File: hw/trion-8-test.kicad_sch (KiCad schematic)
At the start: 4 parts

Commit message: cleanup of trion project
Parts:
- removed H1, H2, H3, H4: Foot FF-13-P3.5X5.5B, proj_footprints:foot_ff-13, symbol Mechanical:MountingHole
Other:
- removed sheet Ethernet
- removed sheet GPS
- removed sheet LED
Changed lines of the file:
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@@
 (kicad_sch (version 20230121) (generator eeschema)
   (paper "A4")
-  (symbol (lib_id "Mechanical:MountingHole") (at 191.77 132.08 0) (unit 1)
-    (in_bom yes) (on_board yes) (dnp no)
-    (property "Reference" "H3" (at 194.31 130.8679 0)
-      (effects (font (size 1.27 1.27)) (justify left))
-    )
-    (property "Value" "Foot FF-13-P3.5X5.5B" (at 180.34 142.24 0)
-      (effects (font (size 1.27 1.27)) (justify left))
-    )
-    (property "Footprint" "proj_footprints:foot_ff-13" (at 191.77 132.08 0)
-      (effects (font (size 1.27 1.27)) hide)
-    )
-    (property "Datasheet" "~" (at 191.77 132.08 0)
-      (effects (font (size 1.27 1.27)) hide)
-    )
-    (property "Part" "FF-13-P3.5X5.5B" (at 191.77 132.08 0)
-      (effects (font (size 1.27 1.27)) hide)
-    )
-    (property "Manufacturer" "Essentra" (at 191.77 132.08 0)
-      (effects (font (size 1.27 1.27)) hide)
-    )
-    (instances
-      (project "trion-8-test"
-        (path "/8c6e15e3-1804-4f03-8a4f-3cb8420d9169"
-          (reference "H3") (unit 1)
-        )
-      )
-    )
-  )
-  (symbol (lib_id "Mechanical:MountingHole") (at 171.45 132.08 0) (unit 1)
-    (in_bom yes) (on_board yes) (dnp no)
-    (property "Reference" "H1" (at 173.99 130.8679 0)
-      (effects (font (size 1.27 1.27)) (justify left))
-    )
-    (property "Value" "Foot FF-13-P3.5X5.5B" (at 160.02 136.525 0)
-      (effects (font (size 1.27 1.27)) (justify left))
-    )
-    (property "Footprint" "proj_footprints:foot_ff-13" (at 171.45 132.08 0)
-      (effects (font (size 1.27 1.27)) hide)
-    )
-    (property "Datasheet" "~" (at 171.45 132.08 0)
-      (effects (font (size 1.27 1.27)) hide)
-    )
-    (property "Part" "FF-13-P3.5X5.5B" (at 171.45 132.08 0)
-      (effects (font (size 1.27 1.27)) hide)
-    )
-    (property "Manufacturer" "Essentra" (at 171.45 132.08 0)
-      (effects (font (size 1.27 1.27)) hide)
-    )
-    (instances
-      (project "trion-8-test"
-        (path "/8c6e15e3-1804-4f03-8a4f-3cb8420d9169"
-          (reference "H1") (unit 1)
-        )
-      )
-    )
-  )
-  (symbol (lib_id "Mechanical:MountingHole") (at 201.295 132.08 0) (unit 1)
-    (in_bom yes) (on_board yes) (dnp no)
-    (property "Reference" "H4" (at 203.835 130.8679 0)
-      (effects (font (size 1.27 1.27)) (justify left))
-    )
-    (property "Value" "Foot FF-13-P3.5X5.5B" (at 189.865 144.78 0)
-      (effects (font (size 1.27 1.27)) (justify left))
-    )
-    (property "Footprint" "proj_footprints:foot_ff-13" (at 201.295 132.08 0)
-      (effects (font (size 1.27 1.27)) hide)
-    )
-    (property "Datasheet" "~" (at 201.295 132.08 0)
-      (effects (font (size 1.27 1.27)) hide)
-    )
-    (property "Part" "FF-13-P3.5X5.5B" (at 201.295 132.08 0)
-      (effects (font (size 1.27 1.27)) hide)
-    )
-    (property "Manufacturer" "Essentra" (at 201.295 132.08 0)
-      (effects (font (size 1.27 1.27)) hide)
-    )
-    (instances
-      (project "trion-8-test"
-        (path "/8c6e15e3-1804-4f03-8a4f-3cb8420d9169"
-          (reference "H4") (unit 1)
-        )
-      )
-    )
-  )
-  (symbol (lib_id "Mechanical:MountingHole") (at 182.245 132.08 0) (unit 1)
-    (in_bom yes) (on_board yes) (dnp no)
-    (property "Reference" "H2" (at 184.785 130.8679 0)
-      (effects (font (size 1.27 1.27)) (justify left))
-    )
-    (property "Value" "Foot FF-13-P3.5X5.5B" (at 170.815 139.7 0)
-      (effects (font (size 1.27 1.27)) (justify left))
-    )
-    (property "Footprint" "proj_footprints:foot_ff-13" (at 182.245 132.08 0)
-      (effects (font (size 1.27 1.27)) hide)
-    )
-    (property "Datasheet" "~" (at 182.245 132.08 0)
-      (effects (font (size 1.27 1.27)) hide)
-    )
-    (property "Part" "FF-13-P3.5X5.5B" (at 182.245 132.08 0)
-      (effects (font (size 1.27 1.27)) hide)
-    )
-    (property "Manufacturer" "Essentra" (at 182.245 132.08 0)
-      (effects (font (size 1.27 1.27)) hide)
-    )
-    (instances
-      (project "trion-8-test"
-        (path "/8c6e15e3-1804-4f03-8a4f-3cb8420d9169"
-          (reference "H2") (unit 1)
-        )
-      )
-    )
-  )
   (sheet (at 96.52 108.585) (size 31.75 34.925) (fields_autoplaced)
     (stroke (width 0.1524) (type solid))
@@
       (project "trion-8-test"
         (path "/8c6e15e3-1804-4f03-8a4f-3cb8420d9169" (page "7"))
-      )
-    )
-  )
-  (sheet (at 162.56 44.45) (size 50.8 30.48) (fields_autoplaced)
-    (stroke (width 0.1524) (type solid))
-    (fill (color 0 0 0 0.0000))
-    (property "Sheetname" "Ethernet" (at 162.56 43.7384 0)
-      (effects (font (size 1.27 1.27)) (justify left bottom))
-    )
-    (property "Sheetfile" "ethernet.kicad_sch" (at 162.56 75.5146 0)
-      (effects (font (size 1.27 1.27)) (justify left top))
-    )
-    (instances
-      (project "trion-8-test"
-        (path "/8c6e15e3-1804-4f03-8a4f-3cb8420d9169" (page "8"))
-      )
-    )
-  )
-  (sheet (at 163.195 85.725) (size 49.53 32.385) (fields_autoplaced)
-    (stroke (width 0.1524) (type solid))
-    (fill (color 0 0 0 0.0000))
-    (property "Sheetname" "GPS" (at 163.195 85.0134 0)
-      (effects (font (size 1.27 1.27)) (justify left bottom))
-    )
-    (property "Sheetfile" "gps.kicad_sch" (at 163.195 118.6946 0)
-      (effects (font (size 1.27 1.27)) (justify left top))
-    )
-    (instances
-      (project "trion-8-test"
-        (path "/8c6e15e3-1804-4f03-8a4f-3cb8420d9169" (page "9"))
       )
     )
@@
       )
     )
-  )
-  (sheet (at 97.79 76.2) (size 33.655 19.685) (fields_autoplaced)
-    (stroke (width 0.1524) (type solid))
-    (fill (color 0 0 0 0.0000))
-    (property "Sheetname" "LED" (at 97.79 75.4884 0)
-      (effects (font (size 1.27 1.27)) (justify left bottom))
-    )
-    (property "Sheetfile" "led.kicad_sch" (at 97.79 96.4696 0)
-      (effects (font (size 1.27 1.27)) (justify left top))
-    )
-    (instances
-      (project "trion-8-test"
-        (path "/8c6e15e3-1804-4f03-8a4f-3cb8420d9169" (page "8"))
-      )
-    )

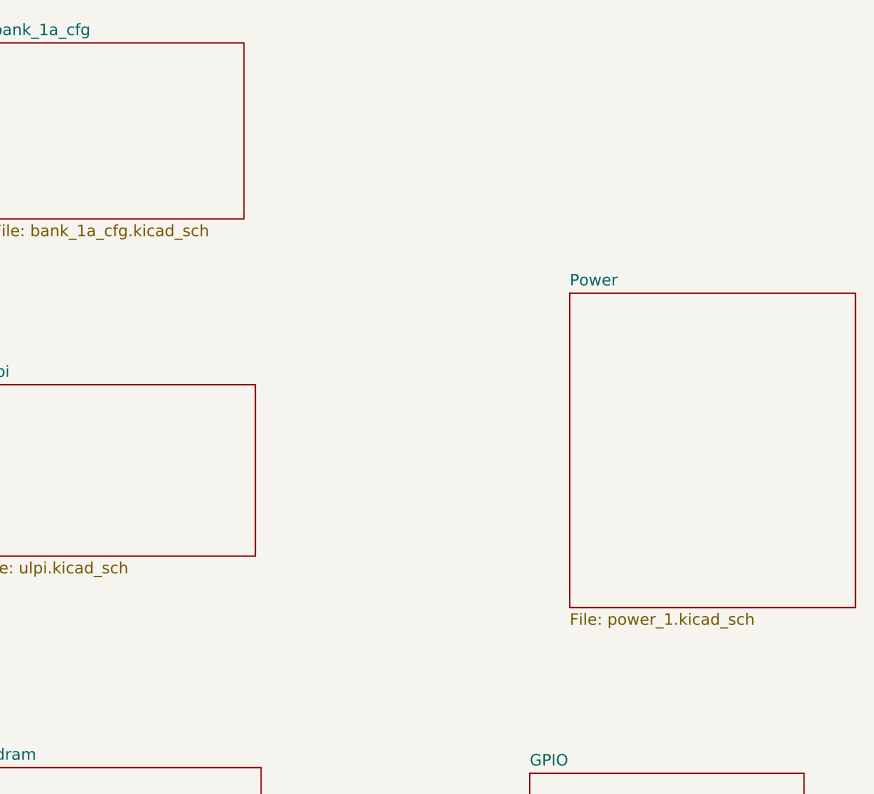
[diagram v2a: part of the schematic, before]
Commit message: layout almost complete with UPLI on the RHS => NO CLOCK INPUT
Have to rework and move the usb transceiver to the left...
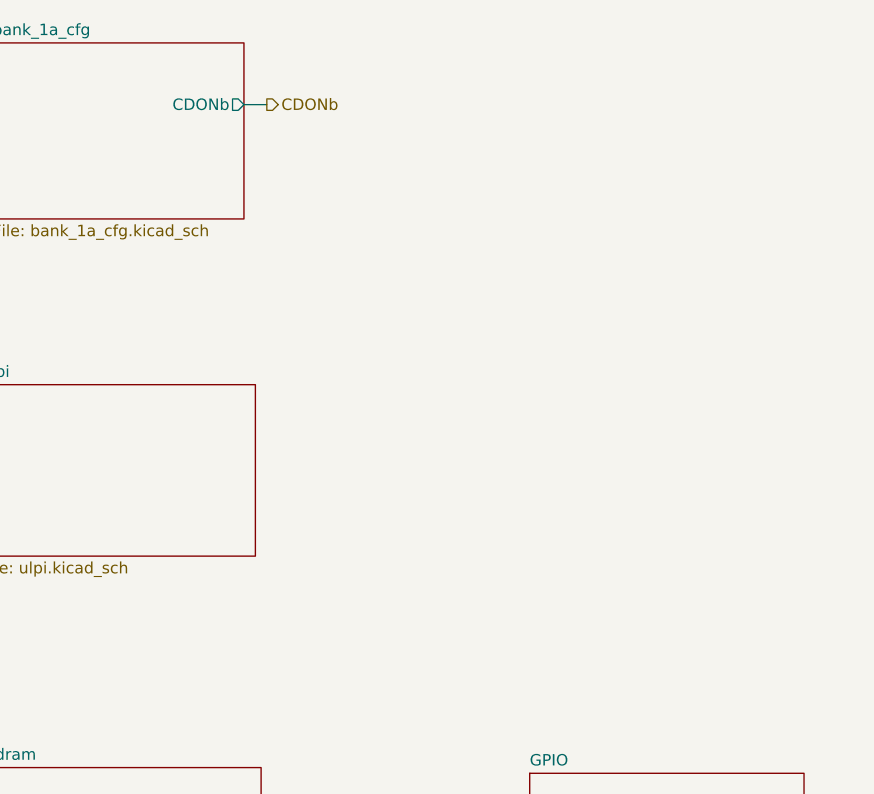
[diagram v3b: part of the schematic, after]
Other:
- removed sheet Power
- sheet bank_1a_cfg ports: added CDONb; removed none
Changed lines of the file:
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@@
 (kicad_sch (version 20230121) (generator eeschema)
   (paper "A4")
-  (sheet (at 96.52 108.585) (size 31.75 34.925) (fields_autoplaced)
-    (stroke (width 0.1524) (type solid))
-    (fill (color 0 0 0 0.0000))
-    (property "Sheetname" "Power" (at 96.52 107.8734 0)
-      (effects (font (size 1.27 1.27)) (justify left bottom))
-    )
-    (property "Sheetfile" "power_1.kicad_sch" (at 96.52 144.0946 0)
-      (effects (font (size 1.27 1.27)) (justify left top))
-    )
-    (instances
-      (project "trion-8-test"
-        (path "/8c6e15e3-1804-4f03-8a4f-3cb8420d9169" (page "7"))
-      )
-      (project "usbadc"
-        (path "/7c8a1f8d-8834-4c9b-aaae-1f231e9b09a1/d9cd2a48-41b0-4b01-a978-0843576735ad" (page "21"))
-      )
-    )
+  (wire (pts (xy 60.325 87.63) (xy 62.865 87.63))
+    (stroke (width 0) (type default))
+  )
+  (hierarchical_label "CDONb" (shape output) (at 62.865 87.63 0) (fields_autoplaced)
+    (effects (font (size 1.27 1.27)) (justify left))
   )
   (sheet (at 31.75 161.29) (size 30.48 24.13) (fields_autoplaced)
@@
       (effects (font (size 1.27 1.27)) (justify left top))
     )
+    (pin "CDONb" output (at 60.325 87.63 0)
+      (effects (font (size 1.27 1.27)) (justify right))
+    )
     (instances

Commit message: finalizing...
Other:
- sheet GPIO renamed bank_4a_4b
- sheet ulpi renamed bank_3a
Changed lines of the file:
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@@
     (stroke (width 0.1524) (type solid))
     (fill (color 0 0 0 0.0000))
-    (property "Sheetname" "ulpi" (at 31.115 118.0334 0)
+    (property "Sheetname" "bank_3a" (at 31.115 118.0334 0)
       (effects (font (size 1.27 1.27)) (justify left bottom))
     )
@@
     (stroke (width 0.1524) (type solid))
     (fill (color 0 0 0 0.0000))
-    (property "Sheetname" "GPIO" (at 92.075 161.2134 0)
+    (property "Sheetname" "bank_4a_4b" (at 92.075 161.2134 0)
       (effects (font (size 1.27 1.27)) (justify left bottom))
     )
